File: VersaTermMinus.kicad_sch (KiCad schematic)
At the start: 58 parts, among them CN1 HDMI_A, CN2 DE15_Socket, CN3 USB_B_Micro, CN5 USB-A, CN6 Mini-DIN-6, CN7 TTL Serial, CN8 DE9 Socket, J2 USBDATA, Q1 2N7002, Q2 2N7002, Q3 2N7002, Q4 2N7002, Q5 2N7002, Q6 2N7002, Q7 2N7002, SW1 RESET, SW2 DEFAULTS, SW3 3V3/5V, U1 Raspberry Pi Pico, U3 MAX3232

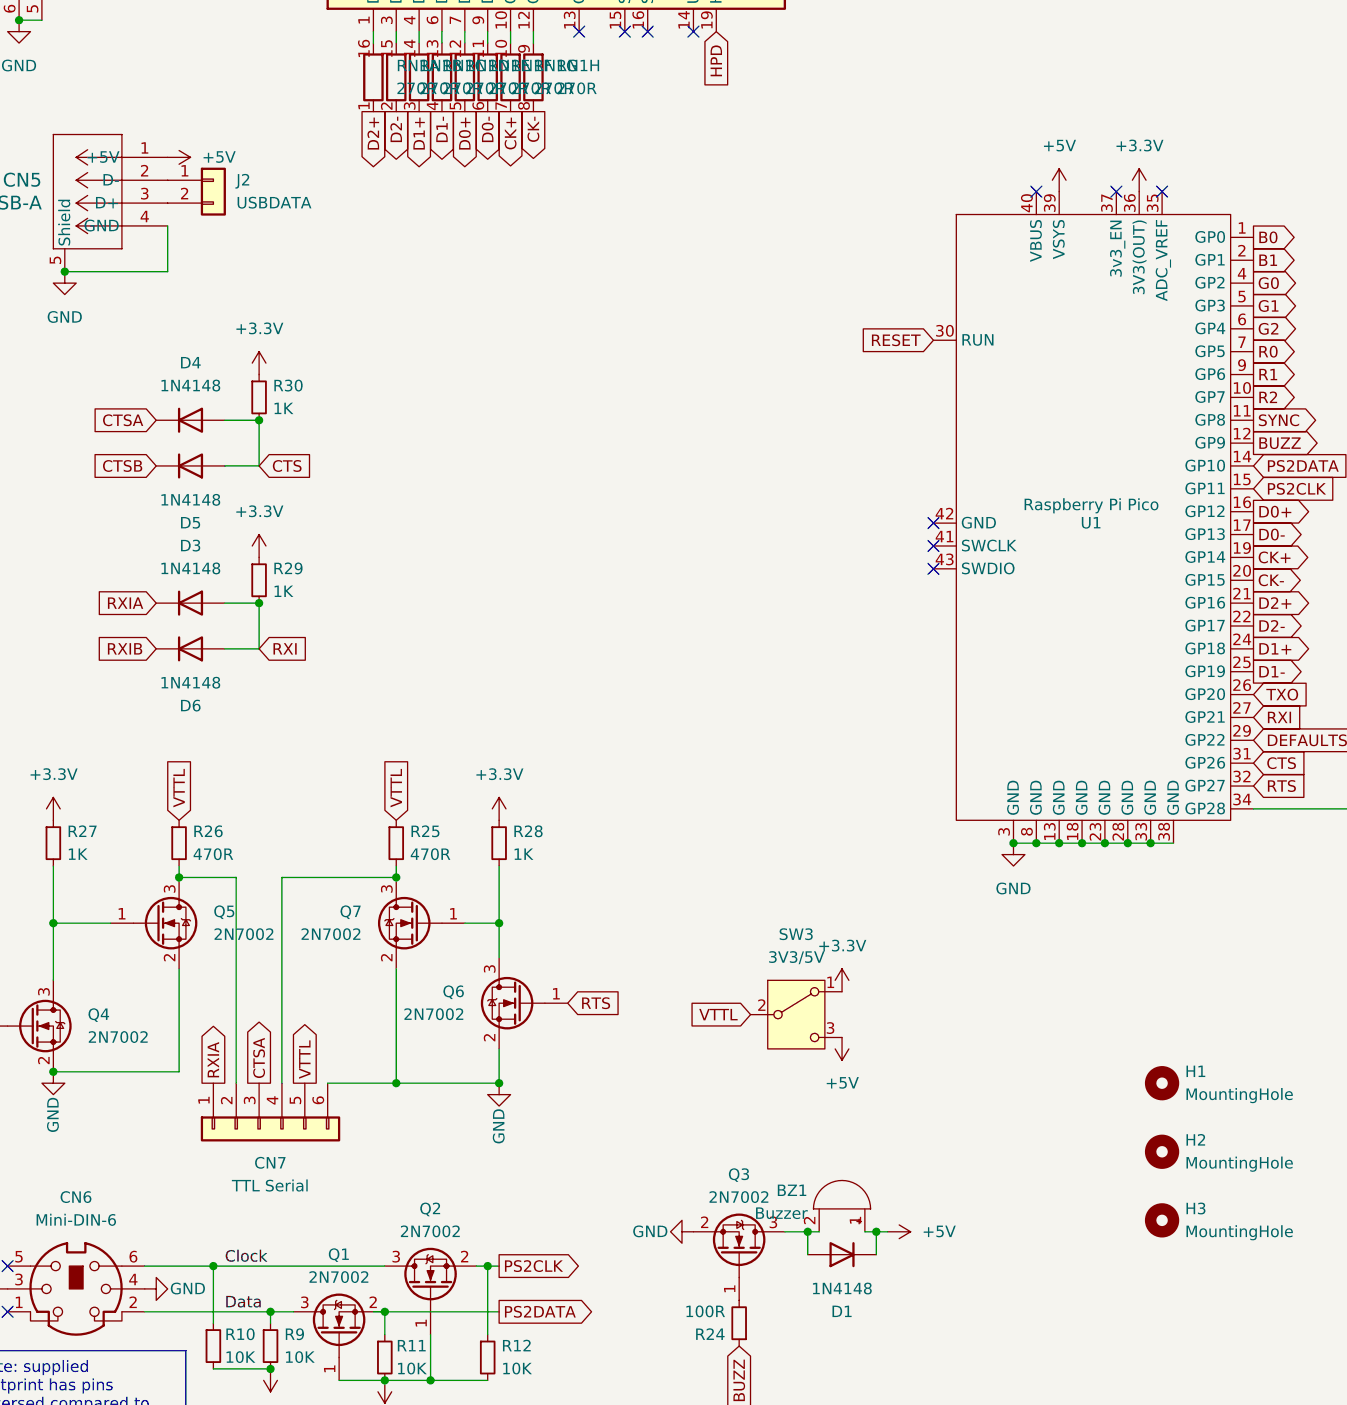
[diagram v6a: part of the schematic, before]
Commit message: update BOM supplier part numbers
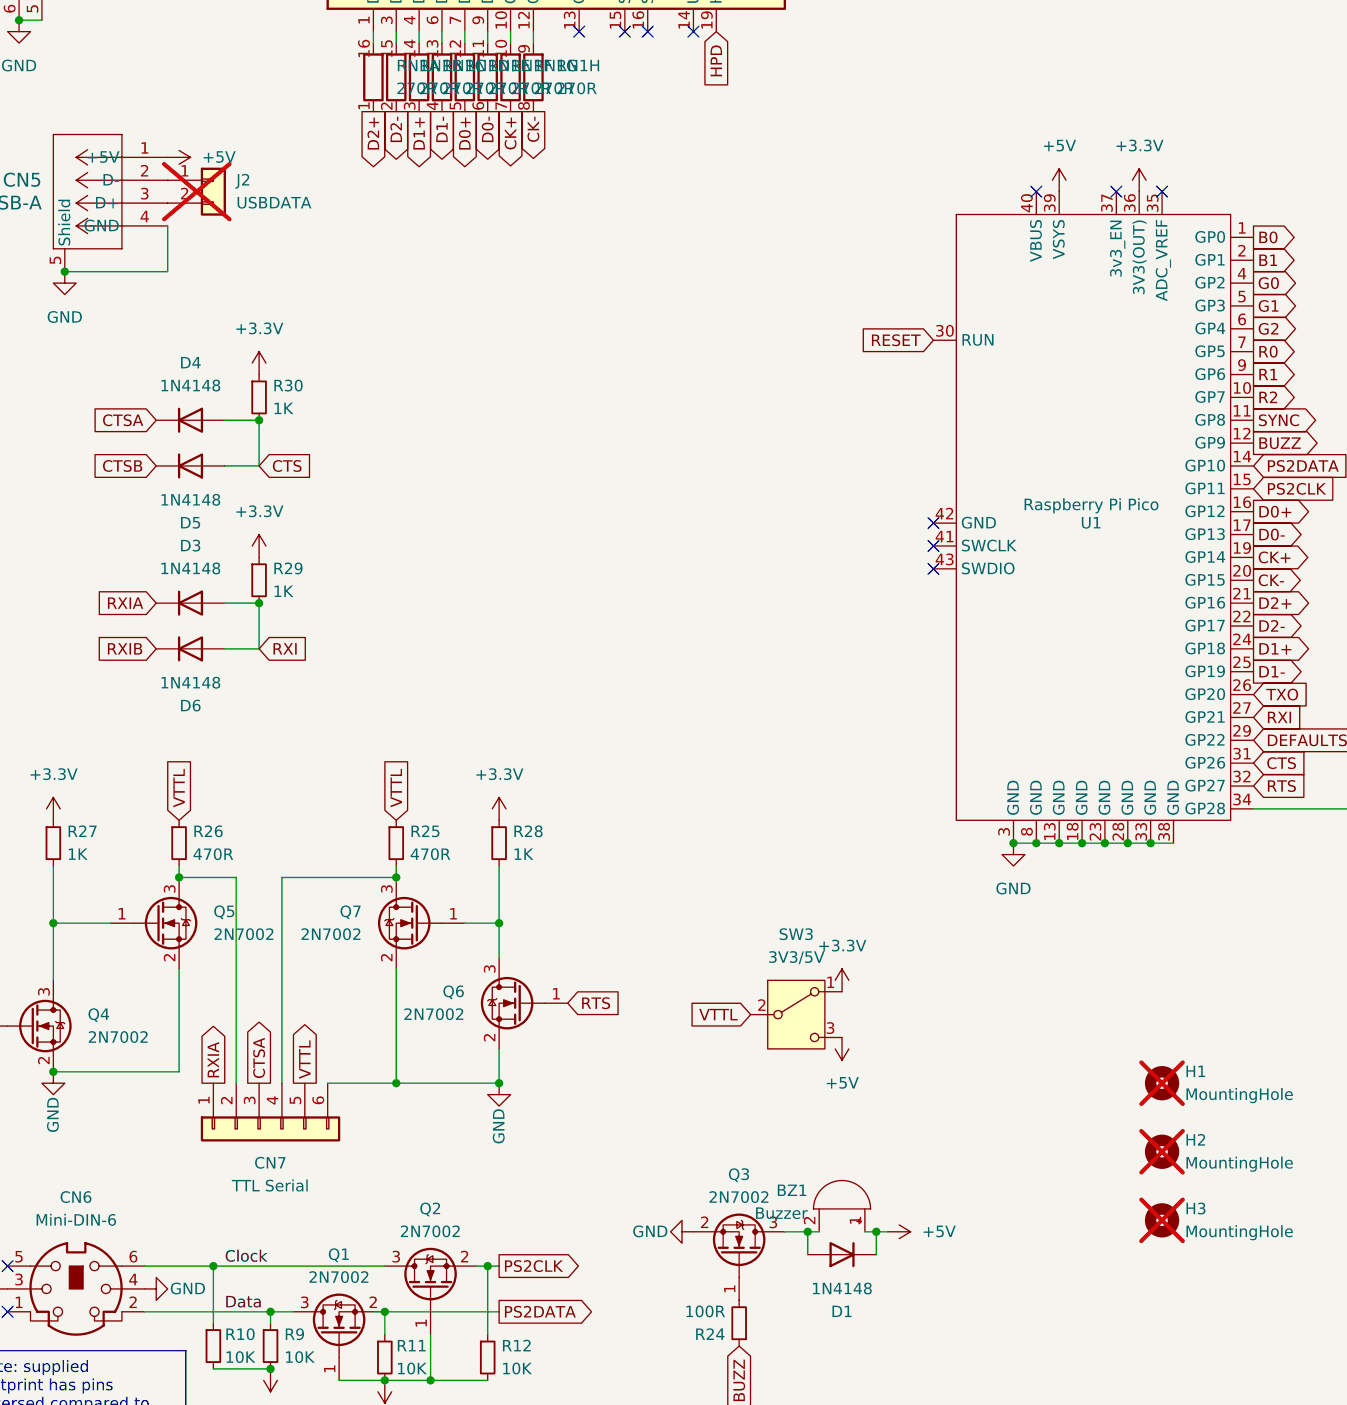
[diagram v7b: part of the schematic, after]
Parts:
- BZ1: LCSC (none) -> C96491
- C3, C4, C5, C6, C7: DigiKey (none) -> 311-1140-1-ND; LCSC (none) -> MBK0805X7R104K500NT
- CN1: LCSC (none) -> C427307
- CN2: LCSC (none) -> C3143144
- CN3: LCSC (none) -> C2874591
- CN5: LCSC (none) -> C293351
- CN6: LCSC (none) -> C77848
- CN7: LCSC (none) -> C492414
- CN8: LCSC (none) -> C141880
- D1, D3, D4, D5, D6: LCSC (none) -> C466656
- D2: LCSC (none) -> C3012747
- H1, H2, H3, J2: now not fitted
- Q1, Q2, Q3, Q4, Q5, Q6, Q7: DigiKey (none) -> 2N7002NCT-ND; LCSC (none) -> C39847032
- R10, R11, R12, R23, R9: LCSC (none) -> C17414
- R15, R18: LCSC (none) -> C17520
- R16, R19, R27, R28, R29, R3, R30: LCSC (none) -> C95781
- R17, R2, R20, R25, R26: DigiKey (none) -> RMCF0805FT470RCT-ND; LCSC (none) -> C5913191
- R21, R24: LCSC (none) -> C105577
- R22: LCSC (none) -> C17673
- RN1: LCSC (none) -> C1731758
- SW1, SW2: LCSC (none) -> C7275163
- SW3: LCSC (none) -> C393937
- U3: LCSC (none) -> C15846
